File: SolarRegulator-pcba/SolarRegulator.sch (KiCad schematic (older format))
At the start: 23 parts, among them J1 USB_B_Micro

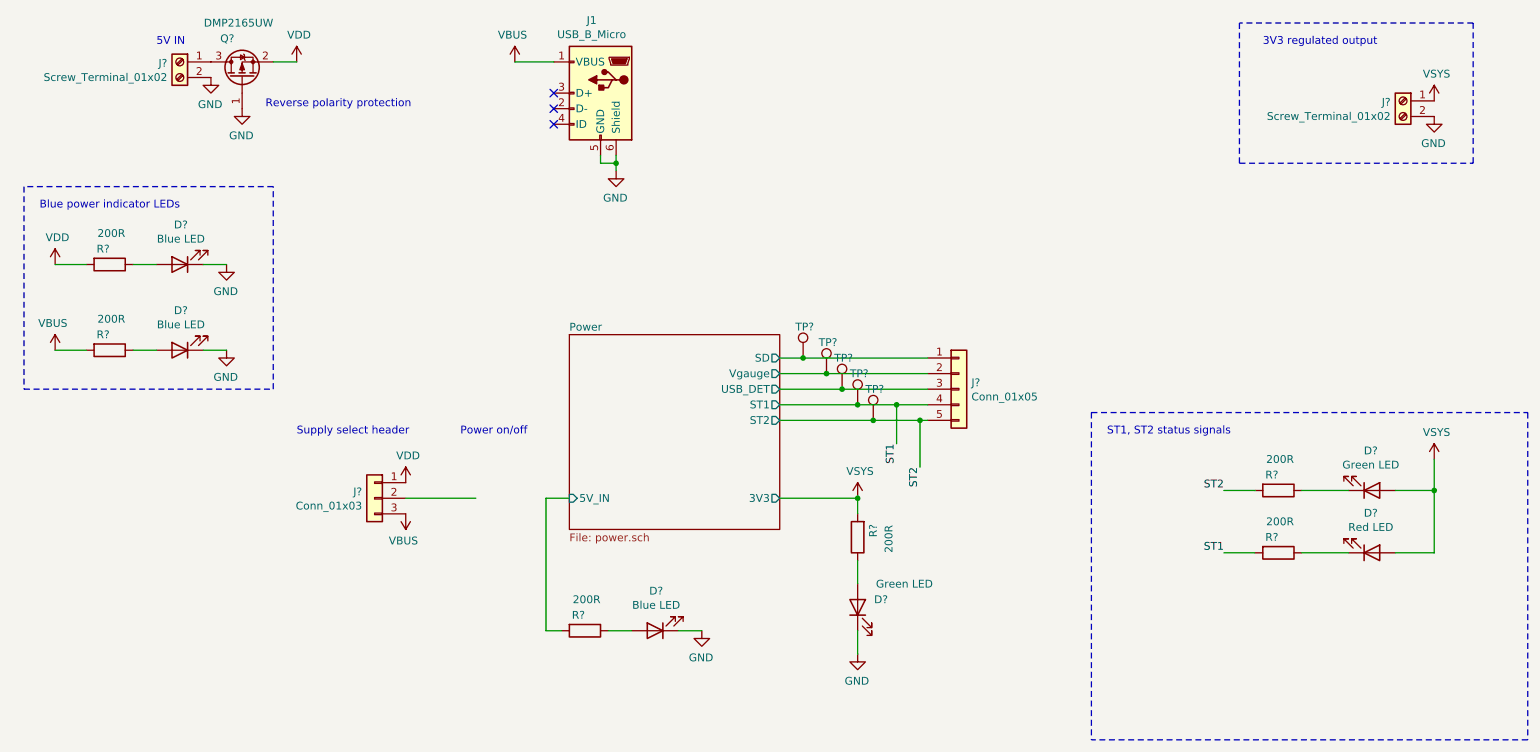
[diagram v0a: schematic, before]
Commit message: Add terminal blocks
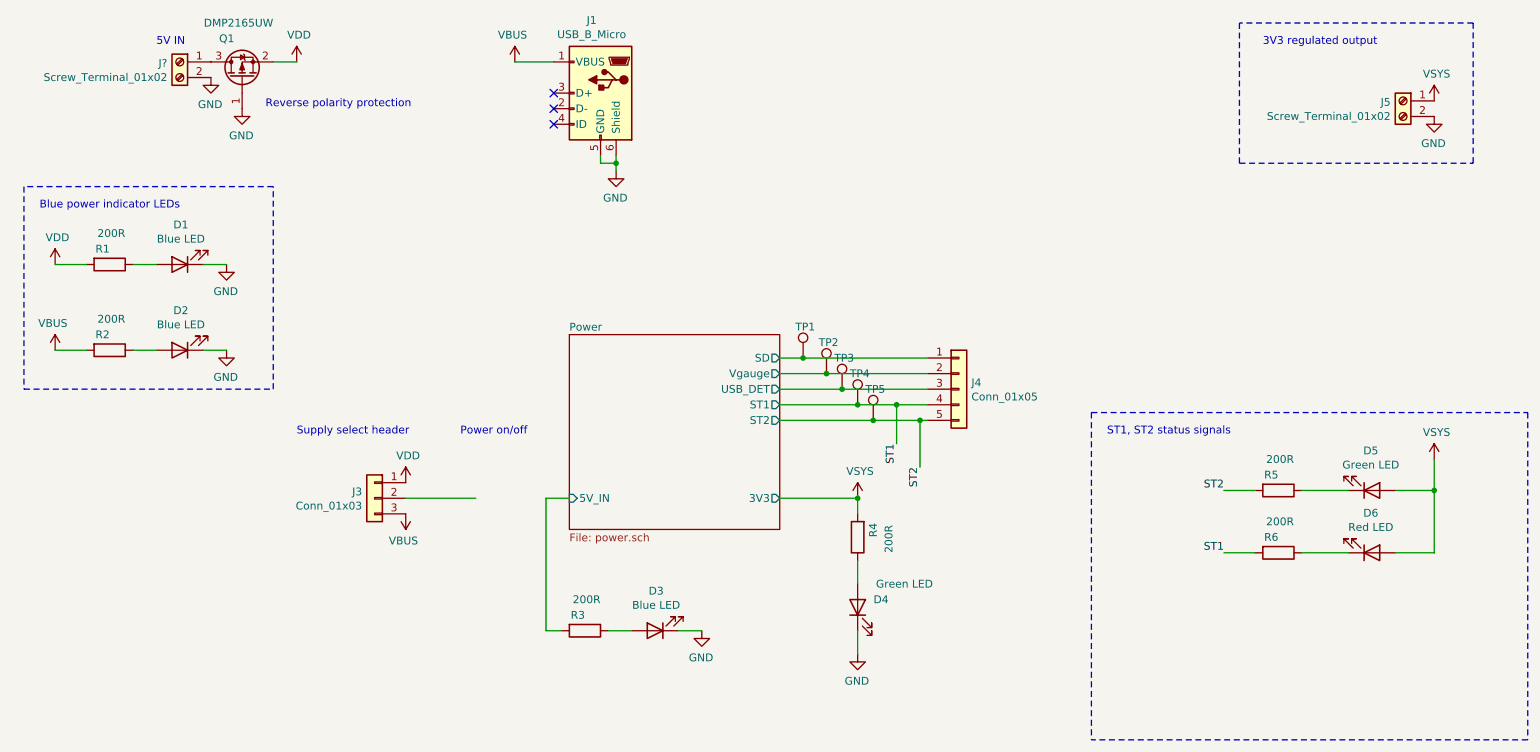
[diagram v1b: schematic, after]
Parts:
- removed J?: Screw_Terminal_01x02, symbol Connector:Screw_Terminal_01x02
- added J?: Screw_Terminal_01x02, TerminalBlock_Phoenix:TerminalBlock_Phoenix_MKDS-1,5-2_1x02_P5.00mm_Horizontal, symbol Connector:Screw_Terminal_01x02
- J5: renamed from J?; footprint (none) -> TerminalBlock_Phoenix:TerminalBlock_Phoenix_MKDS-1,5-2_1x02_P5.00mm_Horizontal
- gave numbers to parts that had none: 20
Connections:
- net GND: now also J?.2 (Pin_2)
- net at Q1.3 (D): now also J?.1 (Pin_1)
